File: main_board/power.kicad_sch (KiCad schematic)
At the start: 29 parts, among them J10 B5B-XH, J11 B5B-XH, J12 B3B-XH, J13 B5B-XH, J8 Conn_01x02, J9 Conn_01x02, Q10 DTC114E, Q9 DTC114E, U12 OKL-T/6-W12N-C, U13 XC6221B302GR, U14 FT232RL, U15 SL2.1A, Y1 12MHz

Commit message: アートワーク : 部品配置
Signed-off-by: Kazuki Iida <elkel53930@gmail.com>
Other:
- moved on the sheet: C31, C33, Q10, Q9

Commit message: アートワーク : 配線完了
Signed-off-by: Kazuki Iida <elkel53930@gmail.com>
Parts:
- J10, J11, J13: footprint Connector_JST:JST_XH_B5B-XH-AM_1x05_P2.50mm_Vertical -> Connector_JST:JST_XH_B5B-XH-A_1x05_P2.50mm_Vertical
- J12: footprint Connector_JST:JST_XH_B3B-XH-AM_1x03_P2.50mm_Vertical -> Connector_JST:JST_XH_B3B-XH-A_1x03_P2.50mm_Vertical
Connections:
- net USB+: now also J12.2 (Pin_2); no longer J12.3 (Pin_3)
- net USB-: now also J12.3 (Pin_3); no longer J12.2 (Pin_2)
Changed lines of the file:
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@@
 	)
 	(label "USB-"
-		(at 90.17 237.49 0)
+		(at 90.17 234.95 0)
 		(effects
 			(font
@@
 	)
 	(label "USB+"
-		(at 90.17 234.95 0)
+		(at 90.17 237.49 0)
 		(effects
 			(font
@@
 			)
 		)
-		(property "Footprint" "Connector_JST:JST_XH_B3B-XH-AM_1x03_P2.50mm_Vertical"
+		(property "Footprint" "Connector_JST:JST_XH_B3B-XH-A_1x03_P2.50mm_Vertical"
 			(at 74.93 237.49 0)
 			(effects
@@
 			)
 		)
-		(property "Footprint" "Connector_JST:JST_XH_B5B-XH-AM_1x05_P2.50mm_Vertical"
+		(property "Footprint" "Connector_JST:JST_XH_B5B-XH-A_1x05_P2.50mm_Vertical"
 			(at 248.92 223.52 0)
 			(effects
@@
 			)
 		)
-		(property "Footprint" "Connector_JST:JST_XH_B5B-XH-AM_1x05_P2.50mm_Vertical"
+		(property "Footprint" "Connector_JST:JST_XH_B5B-XH-A_1x05_P2.50mm_Vertical"
 			(at 280.67 224.79 0)
 			(effects
@@
 			)
 		)
-		(property "Footprint" "Connector_JST:JST_XH_B5B-XH-AM_1x05_P2.50mm_Vertical"
+		(property "Footprint" "Connector_JST:JST_XH_B5B-XH-A_1x05_P2.50mm_Vertical"
 			(at 248.92 254 0)
 			(effects

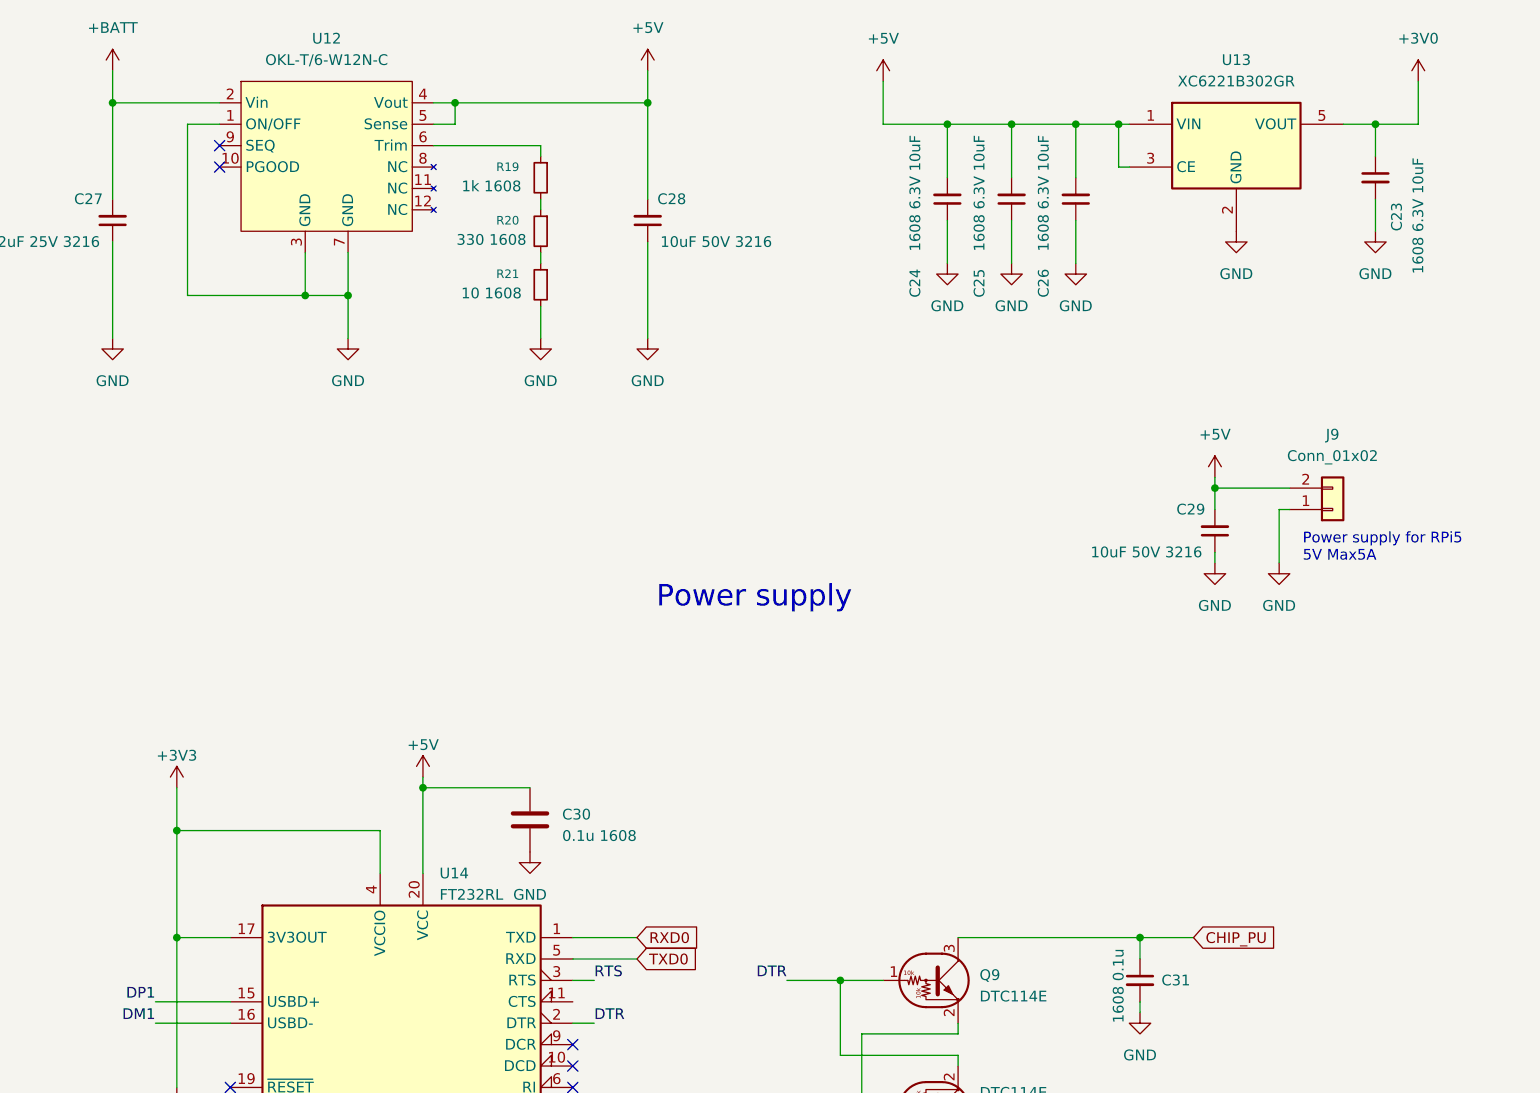
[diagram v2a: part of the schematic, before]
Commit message: 回路図 : 3.0Vから3.3Vに変更 アートワーク : コネクタピン配などのシルクを追加
Signed-off-by: Kazuki Iida <elkel53930@gmail.com>
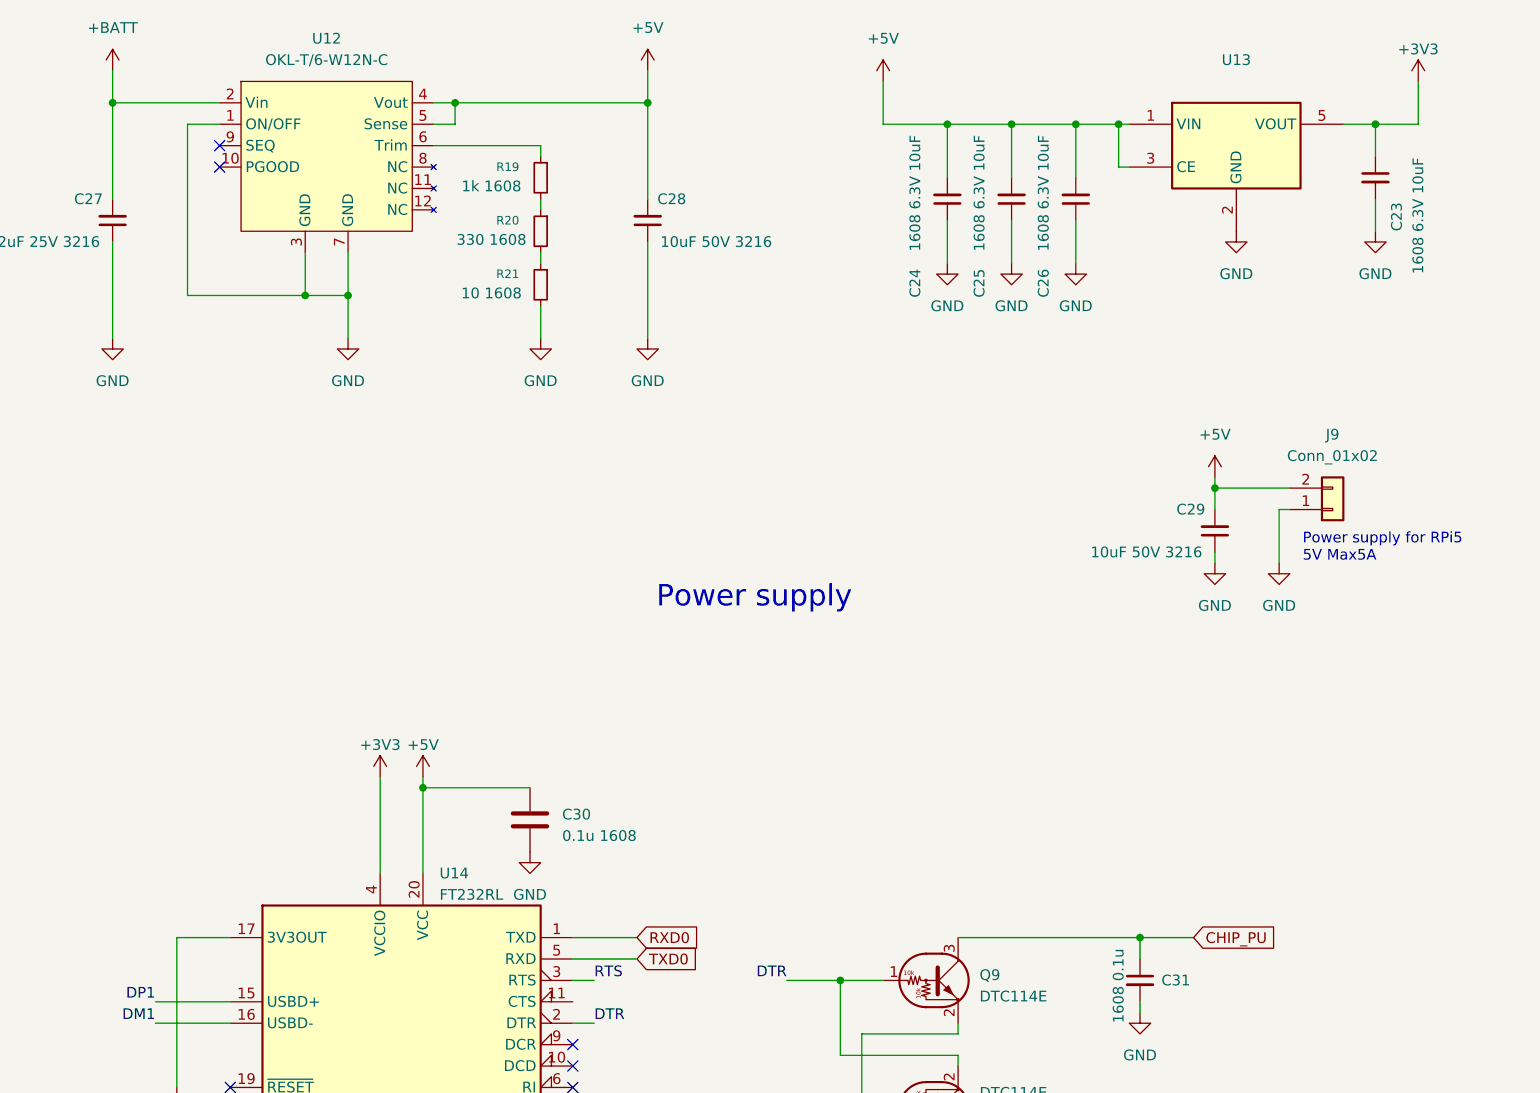
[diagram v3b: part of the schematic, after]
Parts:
- U13: value XC6221B302GR -> XC6221B332MR
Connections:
- net +3V0 is gone; now on net +3V3: C23.1, U13.5 (VOUT)
- net +3V3: no longer C32.1, U14.17 (3V3OUT)
- new net: C32.1, U14.17 (3V3OUT)
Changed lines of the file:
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@@
 	)
 	(junction
-		(at 154.94 133.35)
-		(diameter 0)
-		(color 0 0 0 0)
-	)
-	(junction
 		(at 176.53 176.53)
 		(diameter 0)
@@
 	)
 	(junction
-		(at 154.94 120.65)
-		(diameter 0)
-		(color 0 0 0 0)
-	)
-	(junction
 		(at 246.38 36.83)
 		(diameter 0)
@@
 	(wire
 		(pts
-			(xy 115.57 236.22) (xy 121.92 236.22)
+			(xy 179.07 114.3) (xy 179.07 125.73)
 		)
 		(stroke
@@
 	(wire
 		(pts
-			(xy 179.07 120.65) (xy 154.94 120.65)
+			(xy 115.57 236.22) (xy 121.92 236.22)
 		)
 		(stroke
@@
 	(wire
 		(pts
-			(xy 154.94 115.57) (xy 154.94 120.65)
-		)
-		(stroke
-			(width 0)
-			(type default)
-		)
-	)
-	(wire
-		(pts
 			(xy 246.38 36.83) (xy 254 36.83)
 		)
@@
 	(wire
 		(pts
-			(xy 154.94 120.65) (xy 154.94 133.35)
-		)
-		(stroke
-			(width 0)
-			(type default)
-		)
-	)
-	(wire
-		(pts
 			(xy 115.57 246.38) (xy 121.92 246.38)
 		)
@@
 	(wire
 		(pts
-			(xy 179.07 125.73) (xy 179.07 120.65)
-		)
-		(stroke
-			(width 0)
-			(type default)
-		)
-	)
-	(wire
-		(pts
 			(xy 201.93 133.35) (xy 209.55 133.35)
 		)
@@
 	)
 	(symbol
+		(lib_id "power:+3V3")
+		(at 179.07 114.3 0)
+		(unit 1)
+		(exclude_from_sim no)
+		(in_bom yes)
+		(on_board yes)
+		(dnp no)
+		(property "Reference" "#PWR063"
+			(at 179.07 118.11 0)
+			(effects
+				(font
+					(size 1.27 1.27)
+				)
+				(hide yes)
+			)
+		)
+		(property "Value" "+3V3"
+			(at 179.07 110.49 0)
+			(effects
+				(font
+					(size 1.27 1.27)
+				)
+			)
+		)
+		(property "Footprint" ""
+			(at 179.07 114.3 0)
+			(effects
+				(font
+					(size 1.27 1.27)
+				)
+				(hide yes)
+			)
+		)
+		(property "Datasheet" ""
+			(at 179.07 114.3 0)
+			(effects
+				(font
+					(size 1.27 1.27)
+				)
+				(hide yes)
+			)
+		)
+		(property "Description" ""
+			(at 179.07 114.3 0)
+			(effects
+				(font
+					(size 1.27 1.27)
+				)
+			)
+		)
+		(pin "1"
+		)
+		(instances
+			(project "main_board"
+				(path "/d2cf6a41-8170-4aa9-b19e-2c9825cc9c77/829ce076-7c19-4bad-87be-13e3998cb698"
+					(reference "#PWR063")
+					(unit 1)
+				)
+			)
+		)
+	)
+	(symbol
 		(lib_id "power:GND")
 		(at 148.59 251.46 0)
@@
 			)
 		)
-		(property "Value" "XC6221B302GR"
+		(property "Value" "XC6221B332MR"
 			(at 280.67 31.75 0)
 			(effects
@@
 					(size 1.27 1.27)
 				)
+				(hide yes)
 			)
 		)
@@
 	(symbol
 		(lib_id "power:+3V3")
-		(at 154.94 115.57 0)
+		(at 302.26 31.75 0)
 		(unit 1)
 		(exclude_from_sim no)
@@
 		(dnp no)
 		(property "Reference" "#PWR078"
-			(at 154.94 119.38 0)
+			(at 302.26 35.56 0)
 			(effects
 				(font
@@
 		)
 		(property "Value" "+3V3"
-			(at 154.94 111.76 0)
+			(at 302.26 27.94 0)
 			(effects
 				(font
@@
 		)
 		(property "Footprint" ""
-			(at 154.94 115.57 0)
+			(at 302.26 31.75 0)
 			(effects
 				(font
@@
 		)
 		(property "Datasheet" ""
-			(at 154.94 115.57 0)
+			(at 302.26 31.75 0)
 			(effects
 				(font
@@
 		)
 		(property "Description" ""
-			(at 154.94 115.57 0)
+			(at 302.26 31.75 0)
 			(effects
 				(font
@@
 					(unit 1)
 				)
-			)
-		)
-	)
-	(symbol
-		(lib_id "power:+3V0")
-		(at 302.26 31.75 0)
-		(unit 1)
-		(exclude_from_sim no)
-		(in_bom yes)
-		(on_board yes)
-		(dnp no)
-		(fields_autoplaced yes)
-		(property "Reference" "#PWR063"
-			(at 302.26 35.56 0)
-			(effects
-				(font
-					(size 1.27 1.27)
-				)
-				(hide yes)
-			)
-		)
-		(property "Value" "+3V0"
-			(at 302.26 26.67 0)
-			(effects
-				(font
-					(size 1.27 1.27)
-				)
-			)
-		)
-		(property "Footprint" ""
-			(at 302.26 31.75 0)
-			(effects
-				(font
-					(size 1.27 1.27)
-				)
-				(hide yes)
-			)
-		)
-		(property "Datasheet" ""
-			(at 302.26 31.75 0)
-			(effects
-				(font
-					(size 1.27 1.27)
-				)
-				(hide yes)
-			)
-		)
-		(property "Description" ""
-			(at 302.26 31.75 0)
-			(effects
-				(font
-					(size 1.27 1.27)
-				)
-			)
-		)
-		(pin "1"
-		)
-		(instances
-			(project "main_board"
-				(path "/d2cf6a41-8170-4aa9-b19e-2c9825cc9c77/829ce076-7c19-4bad-87be-13e3998cb698"
-					(reference "#PWR063")
-					(unit 1)
-				)

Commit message: 部品名を修正
Signed-off-by: Kazuki Iida <elkel53930@gmail.com>
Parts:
- C27: value CL31A226KAHNNNE -> 22uF 25V 3216
- C28, C29: value CL31A106KBHNNNE -> 10uF 50V 3216
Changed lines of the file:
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@@
 			)
 		)
-		(property "Value" "CL31A106KBHNNNE"
-			(at 280.67 86.3535 0)
+		(property "Value" "10uF 50V 3216"
+			(at 262.128 87.63 0)
 			(effects
 				(font
@@
 				)
 				(justify right)
-				(hide yes)
 			)
 		)
@@
 					(size 1.27 1.27)
 				)
+				(hide yes)
 			)
 		)
@@
 			)
 		)
-		(property "Value" "CL31A226KAHNNNE"
-			(at 149.86 49.5235 0)
+		(property "Value" "22uF 25V 3216"
+			(at 131.572 50.546 0)
 			(effects
 				(font
@@
 				)
 				(justify right)
-				(hide yes)
 			)
 		)
@@
 					(size 1.27 1.27)
 				)
+				(hide yes)
 			)
 		)
@@
 			)
 		)
-		(property "Value" "CL31A106KBHNNNE"
-			(at 208.28 49.5235 0)
+		(property "Value" "10uF 50V 3216"
+			(at 226.568 50.292 0)
 			(effects
 				(font
@@
 				)
 				(justify right)
-				(hide yes)
 			)
 		)
@@
 					(size 1.27 1.27)
 				)
-			)
-		)
+				(hide yes)
+			)
+		)

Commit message: 定数や型番の修正
Signed-off-by: Kazuki Iida <elkel53930@gmail.com>
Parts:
- added R22: 1608 1k, Resistor_SMD:R_0603_1608Metric, symbol Device:R
- C30, C32: value 0.1u 1608 -> 1608 50V 0.1uF
- C31, C33: value 1608 0.1u -> 1608 50V 0.1uF
- C34, C35: value 10uF -> 10uF 2012
- R19: value 0603WAF1001T5E -> 1k 1608
- R20: value 0603WAF1001T5E -> 330 1608
- R21: value 0603WAF1001T5E -> 10 1608
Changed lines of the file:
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@@
 			)
 		)
-		(property "Value" "0603WAF1001T5E"
+		(property "Value" "10 1608"
 			(at 195.58 57.1499 0)
 			(effects
@@
 				)
 				(justify left)
-				(hide yes)
 			)
 		)
@@
 					(size 1.27 1.27)
 				)
+				(hide yes)
 			)
 		)
@@
 	)
 	(symbol
+		(lib_id "Device:R")
+		(at 176.53 81.28 270)
+		(mirror x)
+		(unit 1)
+		(exclude_from_sim no)
+		(in_bom yes)
+		(on_board yes)
+		(dnp no)
+		(property "Reference" "R22"
+			(at 175.26 83.82 90)
+			(effects
+				(font
+					(size 1.27 1.27)
+				)
+				(justify left)
+			)
+		)
+		(property "Value" "1608 1k"
+			(at 172.72 78.74 90)
+			(effects
+				(font
+					(size 1.27 1.27)
+				)
+				(justify left)
+			)
+		)
+		(property "Footprint" "Resistor_SMD:R_0603_1608Metric"
+			(at 176.53 83.058 90)
+			(effects
+				(font
+					(size 1.27 1.27)
+				)
+				(hide yes)
+			)
+		)
+		(property "Datasheet" "~"
+			(at 176.53 81.28 0)
+			(effects
+				(font
+					(size 1.27 1.27)
+				)
+				(hide yes)
+			)
+		)
+		(property "Description" ""
+			(at 176.53 81.28 0)
+			(effects
+				(font
+					(size 1.27 1.27)
+				)
+			)
+		)
+		(pin "1"
+		)
+		(pin "2"
+		)
+		(instances
+			(project "main_board"
+				(path "/d2cf6a41-8170-4aa9-b19e-2c9825cc9c77/829ce076-7c19-4bad-87be-13e3998cb698"
+					(reference "R22")
+					(unit 1)
+				)
+			)
+		)
+	)
+	(symbol
 		(lib_id "Device:C_Small")
 		(at 278.13 85.09 180)
@@
 			)
 		)
-		(property "Value" "1608 0.1u"
-			(at 266.7 143.51 90)
+		(property "Value" "1608 50V 0.1uF"
+			(at 271.526 141.224 0)
 			(effects
 				(font
@@
 			)
 		)
-		(property "Value" "0.1u 1608"
-			(at 156.21 166.624 90)
+		(property "Value" "1608 50V 0.1uF"
+			(at 156.464 172.466 90)
 			(effects
 				(font
@@
 			)
 		)
-		(property "Value" "1608 0.1u"
-			(at 266.7 168.91 90)
+		(property "Value" "1608 50V 0.1uF"
+			(at 271.272 166.878 0)
 			(effects
 				(font
@@
 			)
 		)
-		(property "Value" "0.1u 1608"
+		(property "Value" "1608 50V 0.1uF"
 			(at 200.66 121.285 0)
 			(effects
@@
 					(size 1.27 1.27)
 				)
-				(hide yes)
 			)
 		)
@@
 			)
 		)
-		(property "Value" "0603WAF1001T5E"
+		(property "Value" "330 1608"
 			(at 195.58 50.7999 0)
 			(effects
@@
 				)
 				(justify left)
-				(hide yes)
 			)
 		)
@@
 			)
 		)
-		(property "Description" "330 1608"
+		(property "Description" ""
 			(at 192.278 50.546 0)
 			(effects
@@
 					(size 1.27 1.27)
 				)
+				(hide yes)
 			)
 		)
@@
 		(on_board yes)
 		(dnp no)
-		(fields_autoplaced yes)
 		(property "Reference" "C34"
 			(at 165.1 240.0362 0)
@@
 			)
 		)
-		(property "Value" "10uF"
-			(at 165.1 242.5762 0)
+		(property "Value" "10uF 2012"
+			(at 165.862 251.968 90)
 			(effects
 				(font
@@
 		(on_board yes)
 		(dnp no)
-		(fields_autoplaced yes)
 		(property "Reference" "C35"
 			(at 175.26 240.0362 0)
@@
 			)
 		)
-		(property "Value" "10uF"
-			(at 175.26 242.5762 0)
+		(property "Value" "10uF 2012"
+			(at 176.53 252.222 90)
 			(effects
 				(font
@@
 			)
 		)
-		(property "Value" "0603WAF1001T5E"
+		(property "Value" "1k 1608"
 			(at 195.58 44.4499 0)
 			(effects
@@
 				)
 				(justify left)
-				(hide yes)
 			)
 		)
@@
 					(size 1.27 1.27)
 				)
+				(hide yes)
 			)
 		)
